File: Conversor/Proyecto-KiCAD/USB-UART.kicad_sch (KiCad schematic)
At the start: 30 parts, among them P14 USB-B, Q5 IRF7425, SW5 Switch, U14 FT232BL, U15 LP2985-3.3, Y1 6 MHz

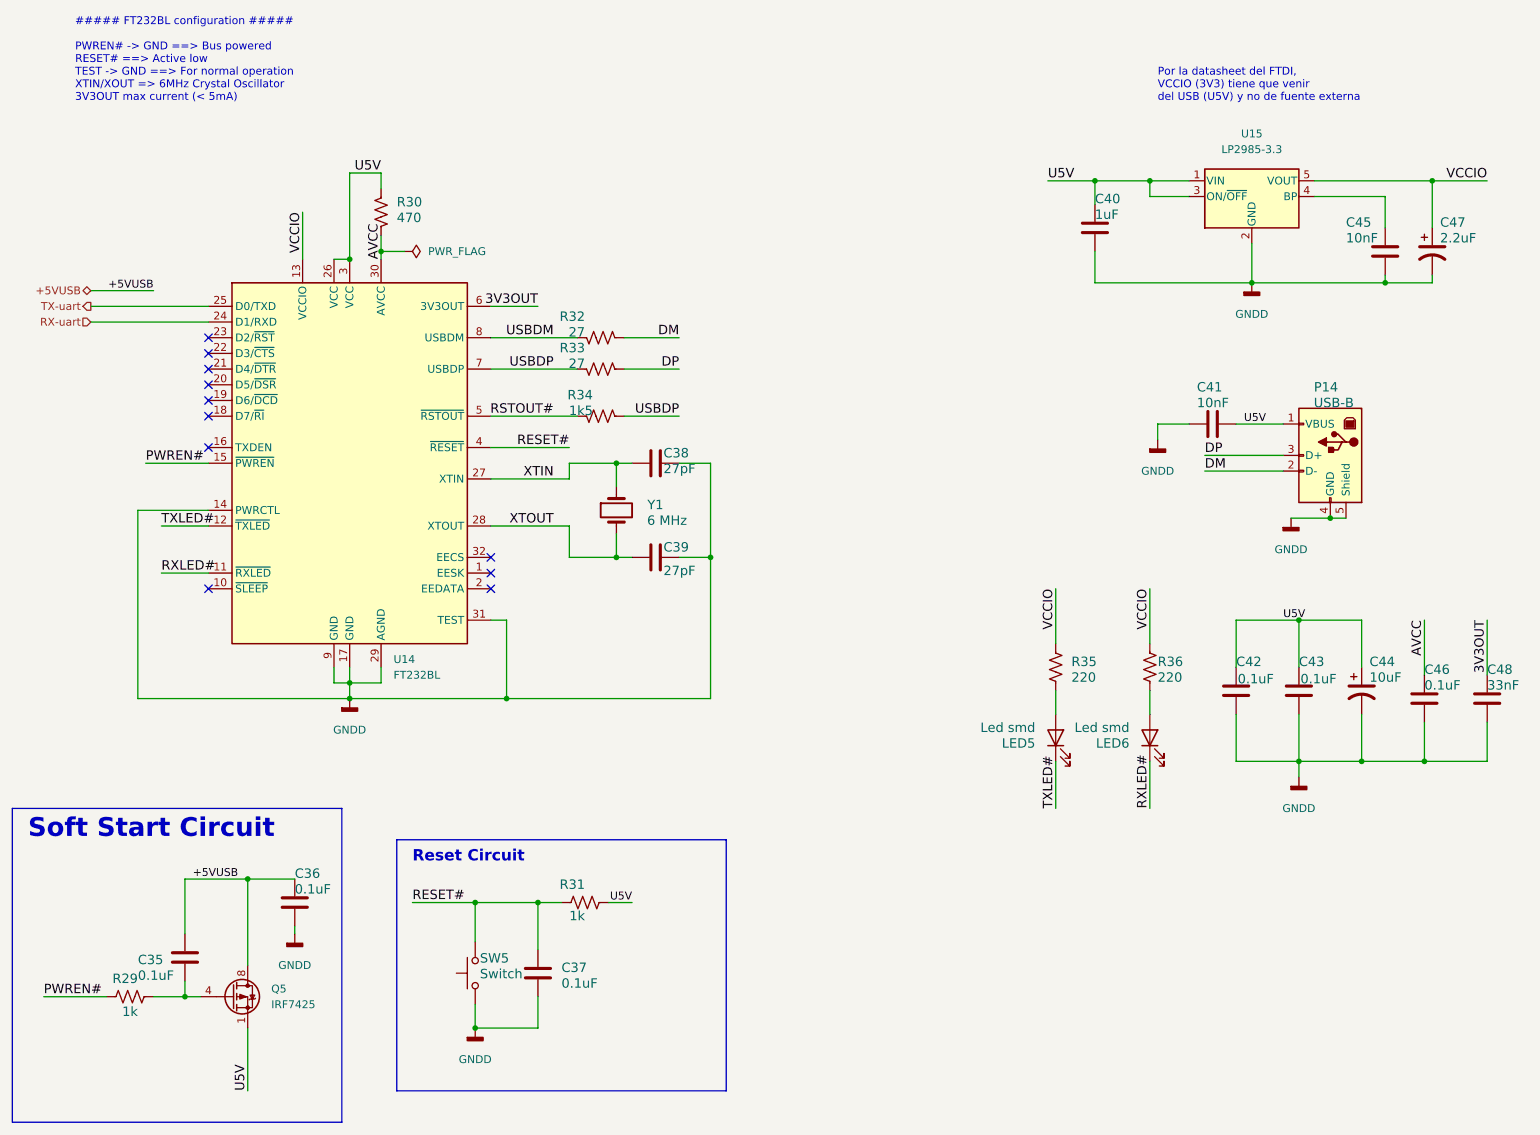
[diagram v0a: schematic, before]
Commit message: Eliminar resistencias de pull-up de SCL y SDAI
- Se pueden remover las Rpu del lado del sensor ya que las Rpu de esas
lineas estan del otro lado (la barrera de aislación proteje de daños).
La de SDAO tiene que quedar por la salida open-drain del LM5056.
- También cambiar las Rpu de 10k a 4k7, porque la capacidad del bus es
muy baja (un solo esclavo y pistas cortas). Así se disminuye es rise
time (Rpu*Cbus) a la mitad.
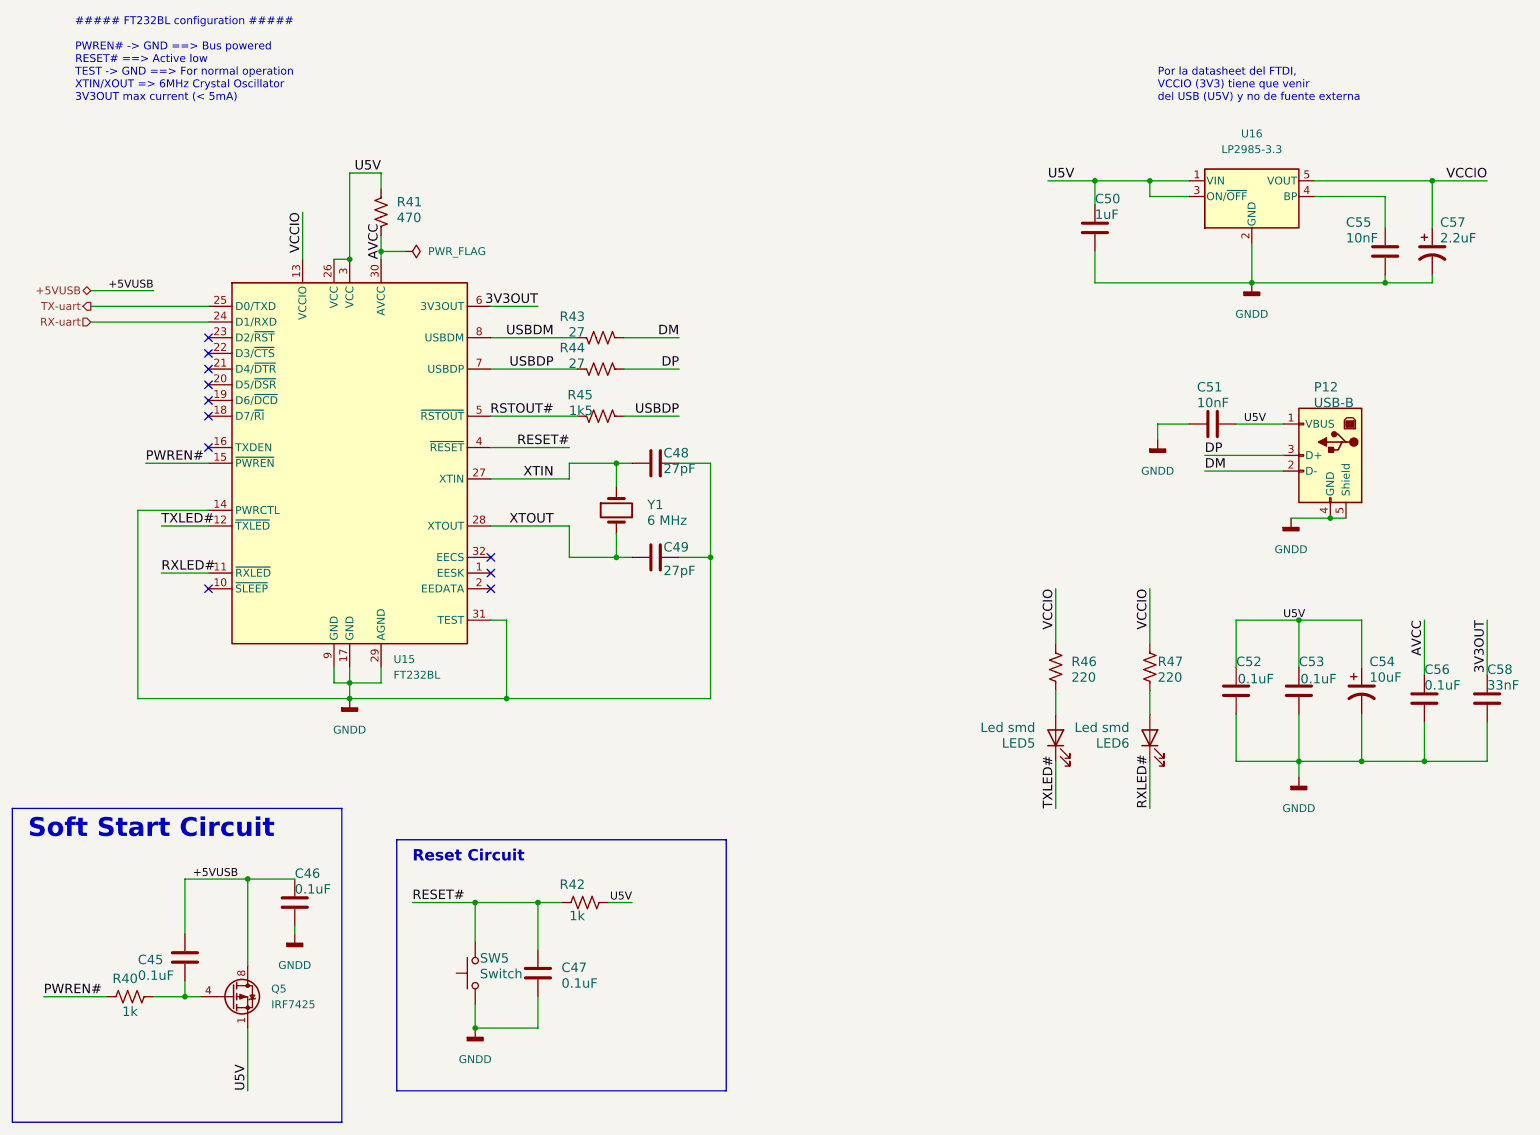
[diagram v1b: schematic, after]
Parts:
- renumbered C35 to C45, C36 to C46, C37 to C47, C38 to C48, C39 to C49, C40 to C50, C41 to C51, C42 to C52, C43 to C53, C44 to C54, C45 to C55, C46 to C56, C47 to C57, C48 to C58, P14 to P12, R29 to R40, R30 to R41, R31 to R42, R32 to R43, R33 to R44, R34 to R45, R35 to R46, R36 to R47, U14 to U15, U15 to U16
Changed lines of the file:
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@@
   (symbol (lib_id "Device:C") (at 123.19 87.63 90) (mirror x) (unit 1)
     (in_bom yes) (on_board yes)
-    (property "Reference" "C38" (id 0) (at 124.46 85.09 90)
+    (property "Reference" "C48" (id 0) (at 124.46 85.09 90)
       (effects (font (size 1.524 1.524)) (justify right top))
     )
@@
   (symbol (lib_id "power:GNDD") (at 226.06 96.52 0) (unit 1)
     (in_bom yes) (on_board yes) (fields_autoplaced)
-    (property "Reference" "#PWR090" (id 0) (at 226.06 102.87 0)
+    (property "Reference" "#PWR098" (id 0) (at 226.06 102.87 0)
       (effects (font (size 1.27 1.27)) hide)
     )
@@
   (symbol (lib_id "Device:R_US") (at 114.3 67.31 270) (mirror x) (unit 1)
     (in_bom yes) (on_board yes)
-    (property "Reference" "R32" (id 0) (at 111.76 64.77 90)
+    (property "Reference" "R43" (id 0) (at 111.76 64.77 90)
       (effects (font (size 1.524 1.524)) (justify right top))
     )
@@
   (symbol (lib_id "power:GNDD") (at 204.47 83.82 0) (unit 1)
     (in_bom yes) (on_board yes) (fields_autoplaced)
-    (property "Reference" "#PWR088" (id 0) (at 204.47 90.17 0)
+    (property "Reference" "#PWR096" (id 0) (at 204.47 90.17 0)
       (effects (font (size 1.27 1.27)) hide)
     )
@@
   (symbol (lib_id "power:GNDD") (at 219.71 58.42 0) (unit 1)
     (in_bom yes) (on_board yes) (fields_autoplaced)
-    (property "Reference" "#PWR089" (id 0) (at 219.71 64.77 0)
+    (property "Reference" "#PWR097" (id 0) (at 219.71 64.77 0)
       (effects (font (size 1.27 1.27)) hide)
     )
@@
   (symbol (lib_id "Device:C") (at 46.99 167.64 0) (unit 1)
     (in_bom yes) (on_board yes)
-    (property "Reference" "C35" (id 0) (at 39.37 168.91 0)
+    (property "Reference" "C45" (id 0) (at 39.37 168.91 0)
       (effects (font (size 1.524 1.524)) (justify left bottom))
     )
@@
   (symbol (lib_id "Device:R_US") (at 187.96 120.65 0) (unit 1)
     (in_bom yes) (on_board yes)
-    (property "Reference" "R35" (id 0) (at 190.5 120.65 0)
+    (property "Reference" "R46" (id 0) (at 190.5 120.65 0)
       (effects (font (size 1.524 1.524)) (justify left bottom))
     )
@@
   (symbol (lib_id "Device:R_US") (at 203.2 120.65 0) (unit 1)
     (in_bom yes) (on_board yes)
-    (property "Reference" "R36" (id 0) (at 204.47 120.65 0)
+    (property "Reference" "R47" (id 0) (at 204.47 120.65 0)
       (effects (font (size 1.524 1.524)) (justify left bottom))
     )
@@
   (symbol (lib_id "Connector:USB_B") (at 232.41 86.36 0) (mirror y) (unit 1)
     (in_bom yes) (on_board yes)
-    (property "Reference" "P14" (id 0) (at 233.68 76.2 0)
+    (property "Reference" "P12" (id 0) (at 233.68 76.2 0)
       (effects (font (size 1.524 1.524)) (justify left bottom))
     )
@@
   (symbol (lib_id "power:GNDD") (at 227.33 138.43 0) (unit 1)
     (in_bom yes) (on_board yes) (fields_autoplaced)
-    (property "Reference" "#PWR091" (id 0) (at 227.33 144.78 0)
+    (property "Reference" "#PWR099" (id 0) (at 227.33 144.78 0)
       (effects (font (size 1.27 1.27)) hide)
     )
@@
   (symbol (lib_id "Device:R_US") (at 114.3 80.01 270) (mirror x) (unit 1)
     (in_bom yes) (on_board yes)
-    (property "Reference" "R34" (id 0) (at 113.03 77.47 90)
+    (property "Reference" "R45" (id 0) (at 113.03 77.47 90)
       (effects (font (size 1.524 1.524)) (justify right top))
     )
@@
   (symbol (lib_id "Device:R_US") (at 78.74 46.99 0) (mirror x) (unit 1)
     (in_bom yes) (on_board yes)
-    (property "Reference" "R30" (id 0) (at 81.28 44.45 0)
+    (property "Reference" "R41" (id 0) (at 81.28 44.45 0)
       (effects (font (size 1.524 1.524)) (justify left bottom))
     )
@@
   (symbol (lib_id "power:GNDD") (at 93.98 179.07 0) (unit 1)
     (in_bom yes) (on_board yes) (fields_autoplaced)
-    (property "Reference" "#PWR087" (id 0) (at 93.98 185.42 0)
+    (property "Reference" "#PWR095" (id 0) (at 93.98 185.42 0)
       (effects (font (size 1.27 1.27)) hide)
     )
@@
   (symbol (lib_id "Device:C") (at 257.81 125.73 180) (unit 1)
     (in_bom yes) (on_board yes)
-    (property "Reference" "C48" (id 0) (at 257.81 121.92 0)
+    (property "Reference" "C58" (id 0) (at 257.81 121.92 0)
       (effects (font (size 1.524 1.524)) (justify right top))
     )
@@
   (symbol (lib_id "Device:R_US") (at 111.76 158.75 90) (unit 1)
     (in_bom yes) (on_board yes)
-    (property "Reference" "R31" (id 0) (at 111.76 154.94 90)
+    (property "Reference" "R42" (id 0) (at 111.76 154.94 90)
       (effects (font (size 1.524 1.524)) (justify left bottom))
     )
@@
   (symbol (lib_id "Device:R_US") (at 38.1 173.99 90) (unit 1)
     (in_bom yes) (on_board yes)
-    (property "Reference" "R29" (id 0) (at 39.37 170.18 90)
+    (property "Reference" "R40" (id 0) (at 39.37 170.18 90)
       (effects (font (size 1.524 1.524)) (justify left bottom))
     )
@@
   (symbol (lib_id "power:GNDD") (at 73.66 125.73 0) (unit 1)
     (in_bom yes) (on_board yes) (fields_autoplaced)
-    (property "Reference" "#PWR086" (id 0) (at 73.66 132.08 0)
+    (property "Reference" "#PWR094" (id 0) (at 73.66 132.08 0)
       (effects (font (size 1.27 1.27)) hide)
     )
@@
   (symbol (lib_id "Regulator_Linear:LP2985-3.3") (at 219.71 44.45 0) (unit 1)
     (in_bom yes) (on_board yes) (fields_autoplaced)
-    (property "Reference" "U15" (id 0) (at 219.71 34.29 0))
+    (property "Reference" "U16" (id 0) (at 219.71 34.29 0))
     (property "Value" "LP2985-3.3" (id 1) (at 219.71 36.83 0))
     (property "Footprint" "Package_TO_SOT_SMD:SOT-23-5" (id 2) (at 219.71 36.195 0)
@@
   (symbol (lib_id "Device:C") (at 194.31 49.53 0) (unit 1)
     (in_bom yes) (on_board yes)
-    (property "Reference" "C40" (id 0) (at 194.31 45.72 0)
+    (property "Reference" "C50" (id 0) (at 194.31 45.72 0)
       (effects (font (size 1.524 1.524)) (justify left bottom))
     )
@@
   (symbol (lib_id "Interface_USB:FT232BM") (at 73.66 87.63 0) (unit 1)
     (in_bom yes) (on_board yes) (fields_autoplaced)
-    (property "Reference" "U14" (id 0) (at 80.7594 119.38 0)
+    (property "Reference" "U15" (id 0) (at 80.7594 119.38 0)
       (effects (font (size 1.27 1.27)) (justify left))
     )
@@
   (symbol (lib_id "Device:C_Polarized_US") (at 237.49 124.46 0) (unit 1)
     (in_bom yes) (on_board yes)
-    (property "Reference" "C44" (id 0) (at 238.76 120.65 0)
+    (property "Reference" "C54" (id 0) (at 238.76 120.65 0)
       (effects (font (size 1.524 1.524)) (justify left bottom))
     )
@@
   (symbol (lib_id "Device:C") (at 227.33 124.46 180) (unit 1)
     (in_bom yes) (on_board yes)
-    (property "Reference" "C43" (id 0) (at 227.33 120.65 0)
+    (property "Reference" "C53" (id 0) (at 227.33 120.65 0)
       (effects (font (size 1.524 1.524)) (justify right top))
     )
@@
   (symbol (lib_id "Device:R_US") (at 114.3 72.39 270) (mirror x) (unit 1)
     (in_bom yes) (on_board yes)
-    (property "Reference" "R33" (id 0) (at 111.76 69.85 90)
+    (property "Reference" "R44" (id 0) (at 111.76 69.85 90)
       (effects (font (size 1.524 1.524)) (justify right top))
     )
@@
   (symbol (lib_id "Device:C_Polarized_US") (at 248.92 53.34 0) (unit 1)
     (in_bom yes) (on_board yes)
-    (property "Reference" "C47" (id 0) (at 250.19 49.53 0)
+    (property "Reference" "C57" (id 0) (at 250.19 49.53 0)
       (effects (font (size 1.524 1.524)) (justify left bottom))
     )
@@
   (symbol (lib_id "Device:C") (at 217.17 124.46 180) (unit 1)
     (in_bom yes) (on_board yes)
-    (property "Reference" "C42" (id 0) (at 217.17 120.65 0)
+    (property "Reference" "C52" (id 0) (at 217.17 120.65 0)
       (effects (font (size 1.524 1.524)) (justify right top))
     )
@@
   (symbol (lib_id "power:GNDD") (at 64.77 163.83 0) (unit 1)
     (in_bom yes) (on_board yes) (fields_autoplaced)
-    (property "Reference" "#PWR085" (id 0) (at 64.77 170.18 0)
+    (property "Reference" "#PWR093" (id 0) (at 64.77 170.18 0)
       (effects (font (size 1.27 1.27)) hide)
     )
@@
   (symbol (lib_id "Device:C") (at 241.3 53.34 0) (unit 1)
     (in_bom yes) (on_board yes)
-    (property "Reference" "C45" (id 0) (at 234.95 49.53 0)
+    (property "Reference" "C55" (id 0) (at 234.95 49.53 0)
       (effects (font (size 1.524 1.524)) (justify left bottom))
     )
@@
   (symbol (lib_id "Device:C") (at 123.19 102.87 90) (mirror x) (unit 1)
     (in_bom yes) (on_board yes)
-    (property "Reference" "C39" (id 0) (at 124.46 100.33 90)
+    (property "Reference" "C49" (id 0) (at 124.46 100.33 90)
       (effects (font (size 1.524 1.524)) (justify right top))
     )
@@
   (symbol (lib_id "Device:C") (at 104.14 170.18 0) (unit 1)
     (in_bom yes) (on_board yes)
-    (property "Reference" "C37" (id 0) (at 107.95 170.18 0)
+    (property "Reference" "C47" (id 0) (at 107.95 170.18 0)
       (effects (font (size 1.524 1.524)) (justify left bottom))
     )
@@
   (symbol (lib_id "Device:C") (at 64.77 158.75 0) (unit 1)
     (in_bom yes) (on_board yes)
-    (property "Reference" "C36" (id 0) (at 64.77 154.94 0)
+    (property "Reference" "C46" (id 0) (at 64.77 154.94 0)
       (effects (font (size 1.524 1.524)) (justify left bottom))
     )
@@
   (symbol (lib_id "Device:C") (at 247.65 125.73 180) (unit 1)
     (in_bom yes) (on_board yes)
-    (property "Reference" "C46" (id 0) (at 247.65 121.92 0)
+    (property "Reference" "C56" (id 0) (at 247.65 121.92 0)
       (effects (font (size 1.524 1.524)) (justify right top))
     )
@@
   (symbol (lib_id "Device:C") (at 213.36 81.28 90) (unit 1)
     (in_bom yes) (on_board yes)
-    (property "Reference" "C41" (id 0) (at 210.82 76.2 90)
-      (effects (font (size 1.524 1.524)) (justify right top))
-    )
+    (property "Reference" "C51" (id 0) (at 210.82 76.2 90)
+      (effects (font (size 1.524 1.524)) (justify right top))
+    )
